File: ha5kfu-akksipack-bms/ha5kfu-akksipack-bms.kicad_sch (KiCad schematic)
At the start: 60 parts, among them IC1 BQ4050RSMR, J1 PACK, J2 PACK1, J3 PACK2, J4 COM, Q1 AON6512, Q2 AON6512, Q3 2N7002, Q4 AO3400A, Q5 AO3400A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

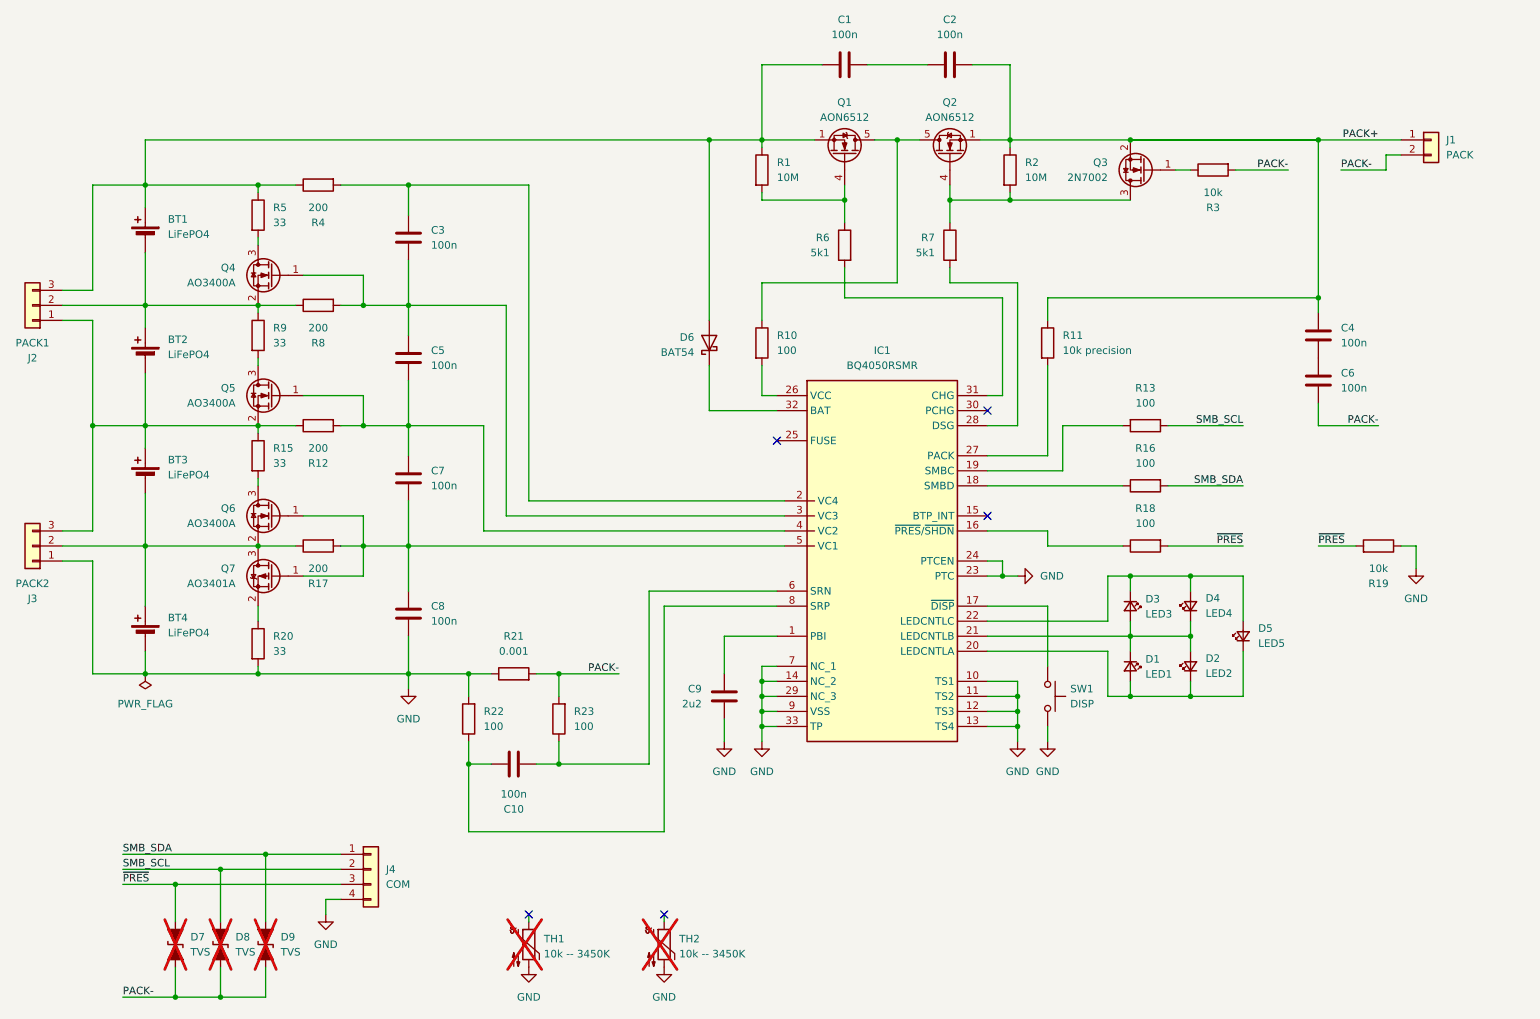
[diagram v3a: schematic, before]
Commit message: Complete PCB, add comments (as documentation) to schematic
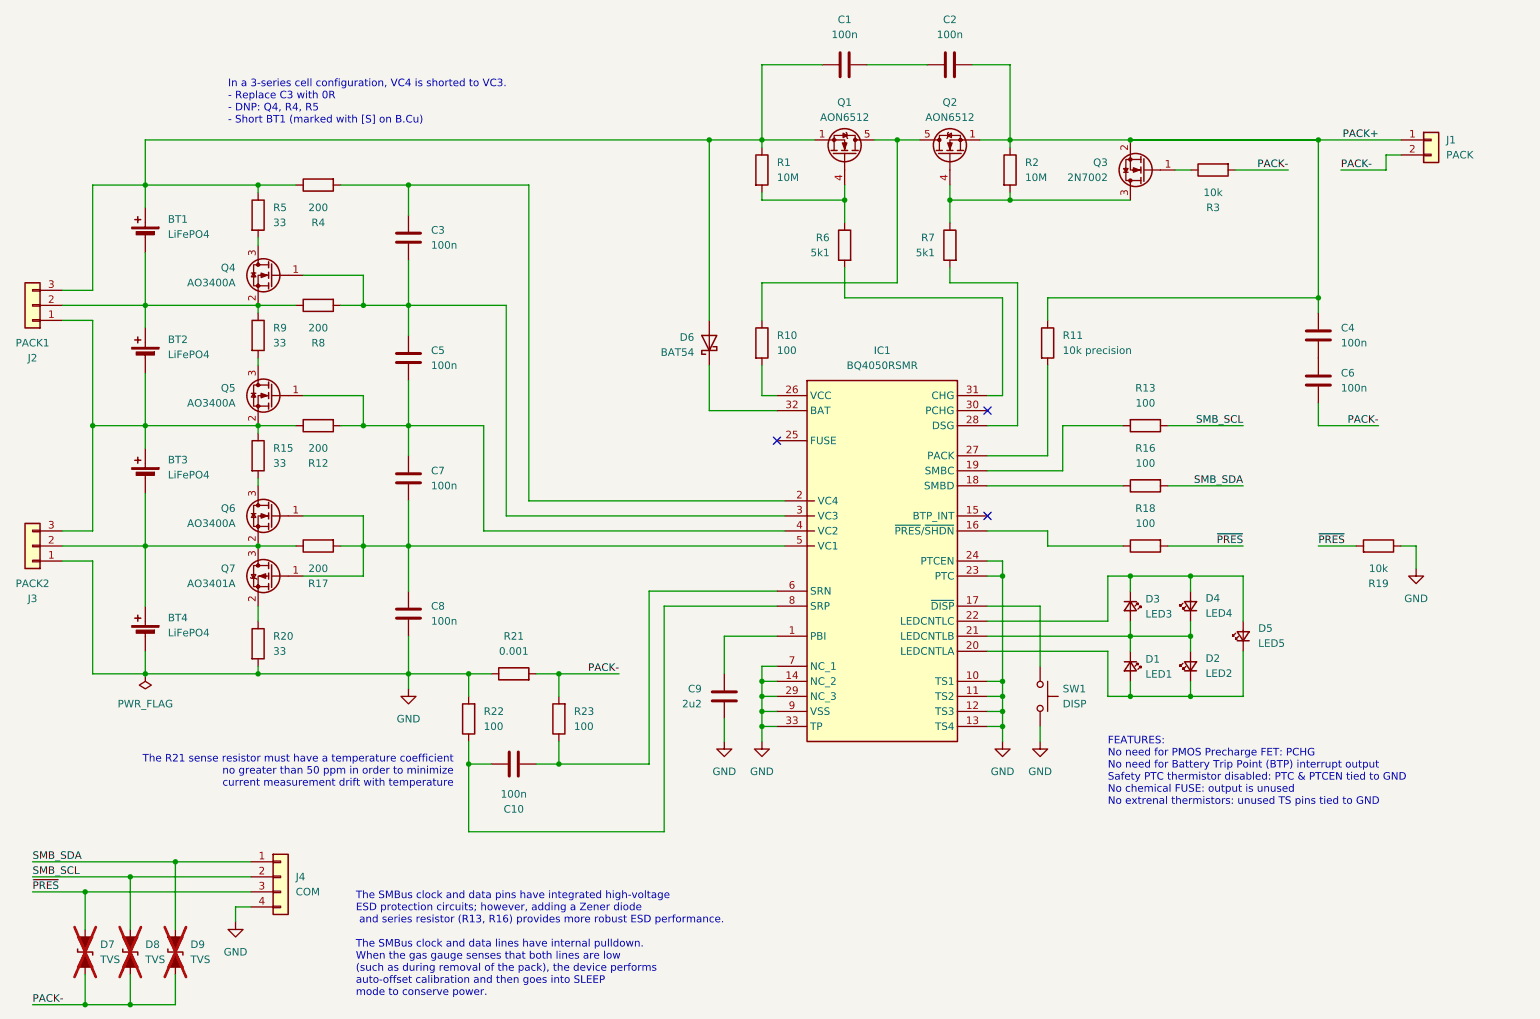
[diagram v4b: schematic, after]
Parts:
- removed TH1, TH2: 10k -- 3450K, Connector_PinHeader_2.54mm:PinHeader_1x02_P2.54mm_Vertical, symbol Device:Thermistor_NTC
- BT1: footprint (none) -> Resistor_SMD:R_0603_1608Metric; now left out of the parts list
- BT2, BT3, BT4, D7, D8, D9: now left out of the parts list
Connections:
- no-connect marks 5 -> 3
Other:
- note added: "FEATURES: No need for PMOS Precharge FET: PCHG No need for Battery Trip Point (BTP) interrupt output Safety PTC thermistor disabled: PTC & PTCEN tied to GND No chemical FUSE: output is unused No extrenal thermistors: unused TS pins tied to GND"
- note added: "In a 3-series cell configuration, VC4 is shorted to VC3. - Replace C3 with 0R - DNP: Q4, R4, R5 - Short BT1 (marked with [S] on B.Cu)"
- note added: "The R21 sense resistor must have a temperature coefficient no greater than 50 ppm in order to minimize current measurement drift with temperature"
- note added: "The SMBus clock and data pins have integrated high-voltage ESD protection circuits; however, adding a Zener diode and series resistor (R13, R16) provides more robust ESD performance. The SMBus clock and data lines have internal pulldown. When the gas gauge senses that both lines are low (such as during removal of the pack), the device performs auto-offset calibration and then goes into SLEEP mode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"
- company: (none) ->   design by HA3PB
- title: (none) -> KAFUPAKK
- moved on the sheet: D7, D8, D9, J4, SW1
